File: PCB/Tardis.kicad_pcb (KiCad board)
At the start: 4 copper layers, 99.1 x 152.4 mm, 143 parts, among them J1 CONN_01X01, J10 CONN_01X01, J11 CONN_01X01, J12 CONN_01X01, J13 CONN_01X01, J14 CONN_01X01, J15 CONN_01X01, J16 CONN_01X01, J2 CONN_01X01, J3 CONN_01X01, J4 CONN_01X01, J5 CONN_01X01, J6 CONN_01X01, J7 CONN_01X01, J8 CONN_01X01, J9 CONN_01X01, Q1 2N3904, Q2 2N3904, Q3 2N3904, Q4 2N3904, Q5 2N3904, Q6 2N3904, Q7 2N3904, U1 L4940, U2 MT8888C, U3 MT8888C, U4 ATMEGA328P-AU, U5 ATMEGA328P-AU, U6 ATMEGA328P-AU, U7 LM324N, U8 TS4990IST, U9 TS4990IST, Y1 3.579545MHz, Y2 3.579545MHz, Y3 Crystal_GND2, Y4 Crystal_GND2, Y5 Crystal_GND2

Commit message: ./
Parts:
- removed R63, R64, R65, R66: 0R, Resistor_THT:R_Axial_DIN0207_L6.3mm_D2.5mm_P2.54mm_Vertical
- added R10: 0R, Resistor_THT:R_Axial_DIN0204_L3.6mm_D1.6mm_P2.54mm_Vertical, F.Cu at (220.5, 34.5)
- added R11: 0R, Resistor_THT:R_Axial_DIN0204_L3.6mm_D1.6mm_P2.54mm_Vertical, F.Cu at (216.4, 34.5)
- added R12: 0R, Resistor_THT:R_Axial_DIN0204_L3.6mm_D1.6mm_P2.54mm_Vertical, F.Cu at (212.3, 34.5)
- added R13: 0R, Resistor_THT:R_Axial_DIN0204_L3.6mm_D1.6mm_P2.54mm_Vertical, F.Cu at (208.3, 34.5)
- C22: moved to B.Cu
- R42, R44, R46, R48, R62: moved to F.Cu
- moved C29 125.9 mm to (184.9, 62.0)
- moved R42 75.0 mm to (220.5, 41.1), turned to 90 degrees
- moved R44 73.8 mm to (216.4, 41.1), turned to 90 degrees
- moved R46 72.9 mm to (212.3, 41.1), turned to 90 degrees
- moved R48 72.3 mm to (208.3, 41.1), turned to 90 degrees
- moved R47 58.1 mm to (210.3, 33.0), turned to 270 degrees
- moved C15 58.1 mm to (148.8, 124.0)
- moved D6 58.1 mm to (148.8, 120.7)
- moved Q7 58.1 mm to (161.8, 114.0)
- moved R50 58.1 mm to (149.4, 114.6)
- moved R51 58.1 mm to (149.4, 116.1)
- moved R53 58.1 mm to (148.8, 122.4)
- moved R56 58.1 mm to (155.7, 124.7)
- moved C11 58.1 mm to (149.4, 118.6)
- moved C14 58.1 mm to (156.5, 110.5)
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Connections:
- R42 pad 2: /GND -> Net-(R10-Pad1)
- R44 pad 2: /GND -> Net-(R11-Pad1)
- R46 pad 2: /GND -> Net-(R12-Pad1)
- R48 pad 2: /GND -> Net-(R13-Pad1)
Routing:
- net BTN1: track 0.00 -> 33.1 mm
- net BTN2: track 0.00 -> 30.2 mm
- net BTN3: track 0.00 -> 25.5 mm
- net ~STBY: track 0.00 -> 23.2 mm, vias 0 -> 2
- net BTN4: track 0.00 -> 22.6 mm
- net /GND: track 36.3 -> 57.6 mm, vias 19 -> 32
- net Net-(D6-Pad2): track 2.79 -> 17.1 mm, vias 1 -> 2
- net +5V: track 29.6 -> 42.9 mm, vias 13 -> 24
- net RXI1: track 0.00 -> 10.7 mm, vias 0 -> 1
- net Net-(U6-Pad7): track 0.00 -> 10.3 mm
- net TX01: track 0.00 -> 10.2 mm, vias 0 -> 1
- net Net-(C21-Pad2): track 0.00 -> 9.92 mm
- net MIC_IN1_P: track 0.00 -> 9.74 mm
- net Net-(C16-Pad2): track 0.00 -> 9.46 mm
- net Net-(C4-Pad2): track 0.00 -> 9.24 mm
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
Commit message: PCB Done. To be reviewed.
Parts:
- removed D10: LED, LEDs:LED_0805_HandSoldering
- removed R9: 330R, Resistors_SMD:R_0603_HandSoldering
- C12, C13, C25: moved to F.Cu
- C27, R4, R5: moved to B.Cu
- moved R7 139.5 mm to (189.7, 51.6), turned to 270 degrees
- moved R8 130.9 mm to (191.5, 51.6), turned to 270 degrees
- moved C28 130.3 mm to (196.6, 49.0), turned to 180 degrees
- moved C27 114.1 mm to (198.6, 61.2)
- moved C24 101.3 mm to (233.7, 47.5), turned to 90 degrees
- moved R14 82.6 mm to (254.5, 28.4)
- moved R2 79.2 mm to (190.5, 112.5), turned to 270 degrees
- moved R3 78.0 mm to (202.2, 110.0), turned to 180 degrees
- moved R1 76.8 mm to (189.0, 112.5), turned to 270 degrees
- moved D8 68.3 mm to (201.9, 108.2)
- moved C14 60.3 mm to (207.3, 78.0)
- moved C15 60.3 mm to (199.6, 91.4)
- moved D6 60.3 mm to (199.6, 88.1)
- moved Q7 60.3 mm to (212.6, 81.5)
- moved R53 60.3 mm to (199.6, 89.9)
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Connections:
- H2 pad 1: MIC_IN1_P_RAW -> SPKR_OUT2_P_RAW
- H2 pad 2: SPKR_OUT2_P_RAW -> MIC_IN1_P_RAW
- U6 pad 2: Fona_RST -> Fona_Rx
- U6 pad 32: Fona_Rx -> Fona_RST
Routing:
- net RST: track 14.5 -> 143.7 mm, vias 0 -> 5
- net SCL: track 3.09 -> 130.6 mm, vias 0 -> 5
- net SDA: track 3.27 -> 127.5 mm, vias 0 -> 5
- net SPKR_OUT2_P_RAW: track 13.0 -> 112.7 mm, vias 0 -> 1
- net Fona_Tx: track 0.00 -> 91.1 mm, vias 0 -> 2
- net Fona_Rx: track 0.00 -> 87.5 mm, vias 0 -> 2
- net Fona_RST: track 0.00 -> 85.7 mm
- net LED5: track 0.00 -> 68.9 mm, vias 0 -> 2
- net uC_PTT: track 3.92 -> 67.8 mm, vias 0 -> 1
- net LED4: track 0.00 -> 61.0 mm, vias 0 -> 2
- net SPKR_OUT1_P: track 7.61 -> 66.1 mm, vias 0 -> 2
- net LED3: track 0.00 -> 53.5 mm, vias 0 -> 2
- net LED2: track 0.00 -> 46.0 mm, vias 0 -> 2
- net LED1: track 0.00 -> 37.5 mm
- net +5V: track 42.9 -> 80.0 mm, vias 24 -> 35
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- added copper zone on In1.Cu, net +5V
- added copper zone on In2.Cu, net /GND
- removed copper zone on In2.Cu, net +5V
- removed copper zone on In1.Cu, net /GND

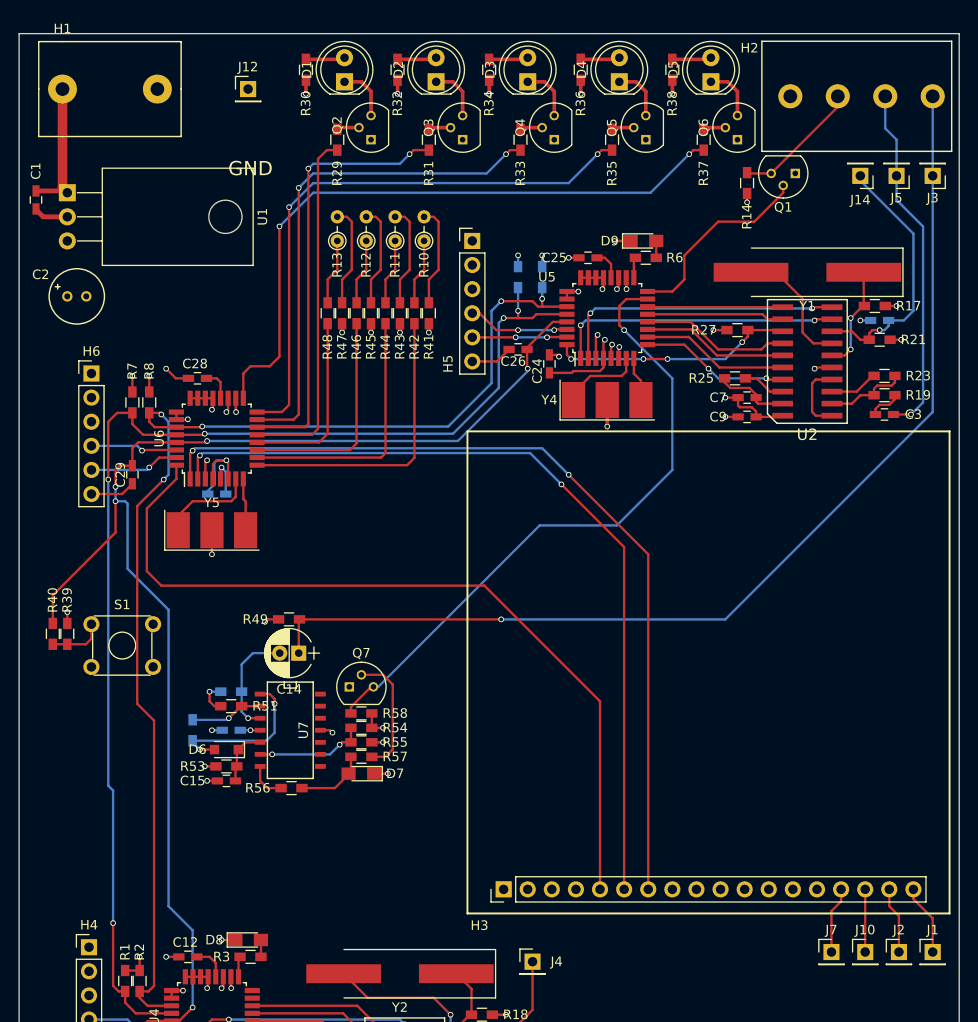
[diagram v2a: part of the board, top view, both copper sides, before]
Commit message: added 0.15inch clearance to edges
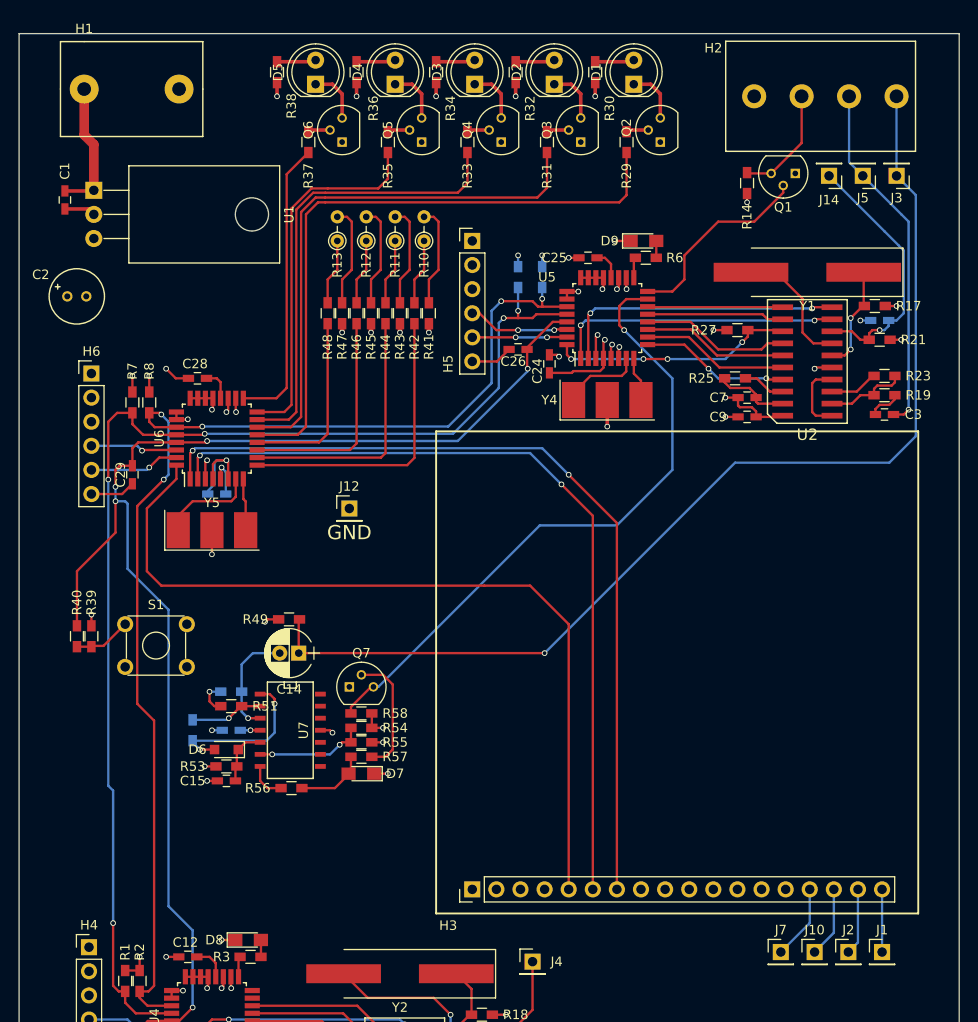
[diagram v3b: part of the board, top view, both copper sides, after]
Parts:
- moved J12 45.5 mm to (212.6, 62.7)
- moved D5 41.7 mm to (209.0, 18.0)
- moved R37 41.7 mm to (208.3, 24.1)
- moved Q6 41.7 mm to (211.8, 24.1)
- moved R38 41.7 mm to (205.0, 16.8)
- moved Q2 30.5 mm to (245.4, 24.1)
- moved D1 30.5 mm to (242.6, 18.0)
- moved R29 30.5 mm to (241.8, 24.1)
- moved R30 30.5 mm to (238.5, 16.8)
- moved Q5 23.6 mm to (220.2, 24.1)
- moved D4 23.6 mm to (217.4, 18.0)
- moved R35 23.6 mm to (216.7, 24.1)
- moved R36 23.6 mm to (213.4, 16.8)
- moved D2 12.4 mm to (234.2, 18.0)
- moved Q3 12.4 mm to (237.0, 24.1)
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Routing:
- net LED5: track 68.9 -> 30.8 mm, vias 2 -> 0
- net LED1: track 37.5 -> 67.0 mm
- net LED4: track 61.0 -> 38.9 mm, vias 2 -> 0
- net LED2: track 46.0 -> 57.4 mm, vias 2 -> 0
- net LED3: track 53.5 -> 48.2 mm, vias 2 -> 0
- net SPKR_OUT2_P_RAW: track 112.7 -> 114.8 mm
- net PTT_OUT: track 13.6 -> 12.0 mm
- net Fona_RST: track 85.7 -> 87.2 mm
- net Fona_Tx: track 91.1 -> 89.8 mm
- net Fona_Rx: track 87.5 -> 86.2 mm
- net MIC_IN2_P: track 7.02 -> 7.87 mm
- net SPKR_OUT1_N_RAW: track 7.45 -> 6.60 mm
- net MIC_IN2_N: track 6.60 -> 7.45 mm
- net RST: track 143.7 -> 142.9 mm
